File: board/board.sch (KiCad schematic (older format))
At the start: 22 parts, among them CON1 NRF24L01+MODULE, CON2 AVR-ISP-6, IC1 ATMEGA88PA-A, SW1 SW_PUSH, U1 XR1151

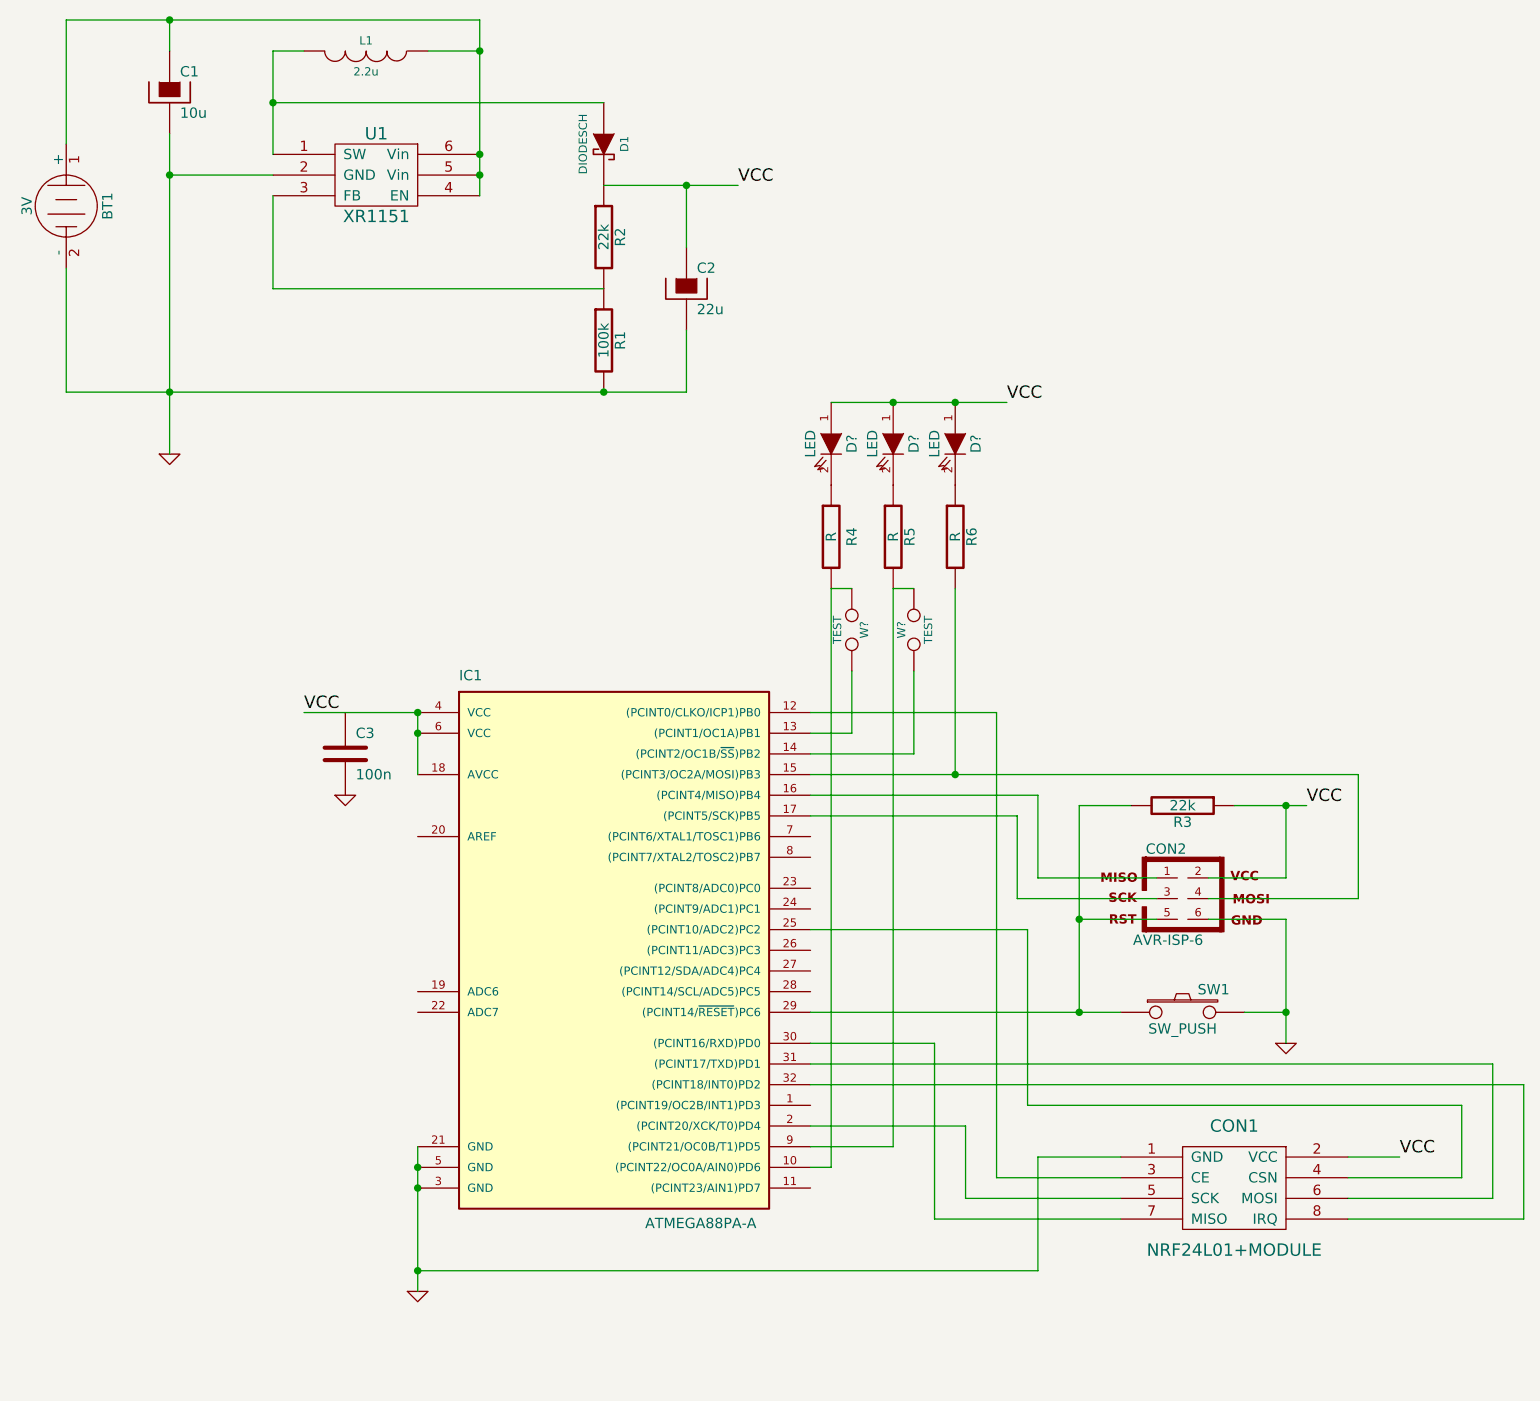
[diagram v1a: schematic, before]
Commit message: Replaced the 3 LEDs with a single 3-colour one
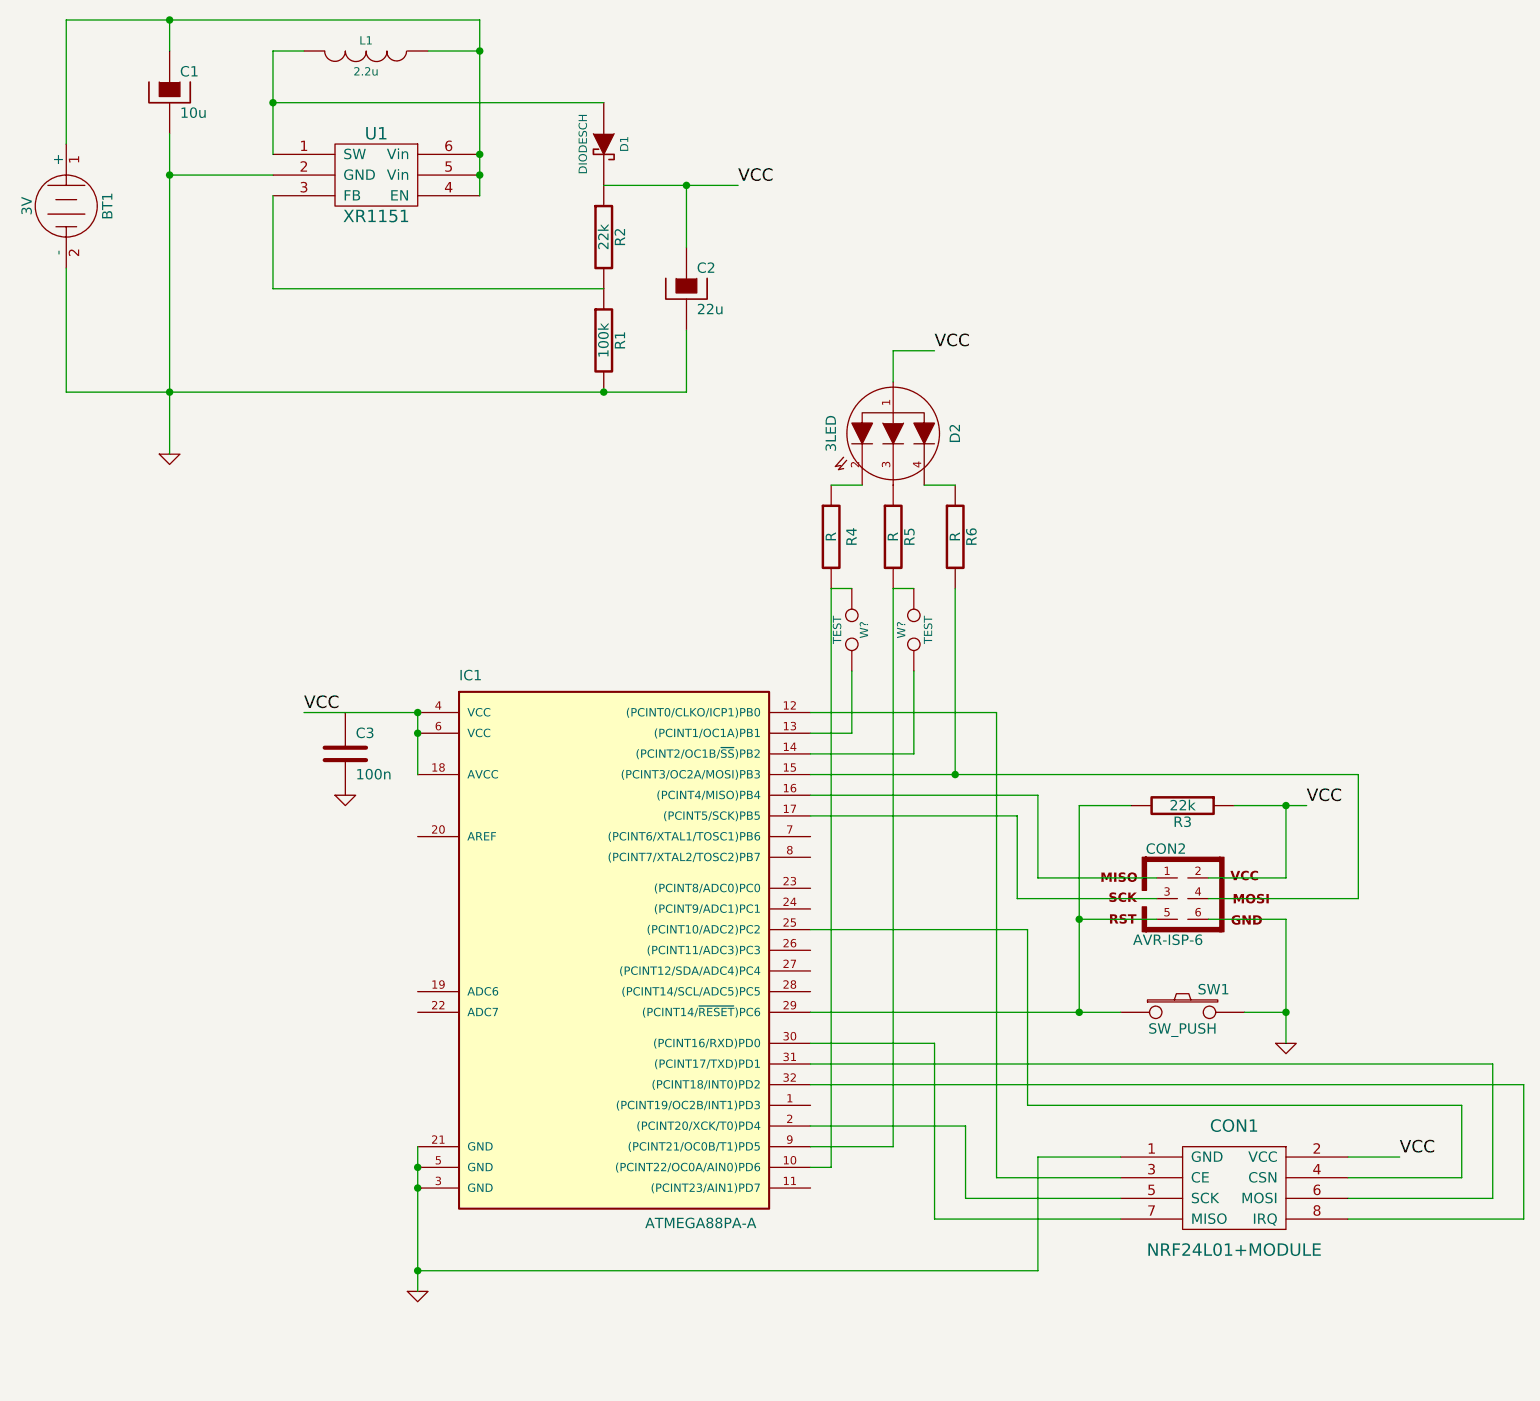
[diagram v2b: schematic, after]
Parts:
- removed D? (x3): LED, symbol LED
- added D2: 3LED, symbol 3LED
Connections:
- net VCC: now also D2.1 (A)
- net at R4.1: now also D2.2 (R)
- net at R5.1: now also D2.3 (G)
- net at R6.1: now also D2.4 (B)
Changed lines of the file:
@@
-EESchema Schematic File Version 2  date Tue 25 Mar 2014 21:10:04 CST
+EESchema Schematic File Version 2  date Tue 25 Mar 2014 21:40:07 CST
 LIBS:power
 LIBS:device
@@
 LIBS:nrf24l01+module
 LIBS:xr1151
+LIBS:3led
 LIBS:board-cache
 EELAYER 25  0
@@
 $EndDescr
 Wire Wire Line
-	4600 4650 5100 4650
-Wire Wire Line
-	5100 4650 5100 4250
-Wire Wire Line
-	5100 3850 5000 3850
-Wire Wire Line
-	4800 4250 4800 4550
-Wire Wire Line
-	4800 4550 4600 4550
-Wire Wire Line
-	4600 5500 5650 5500
-Wire Wire Line
-	5650 5500 5650 6350
-Wire Wire Line
-	5650 6350 7750 6350
-Wire Wire Line
-	7750 6350 7750 6700
+	5200 2700 5000 2700
+Wire Wire Line
+	5000 2700 5000 2850
+Wire Wire Line
+	4850 3350 4700 3350
+Wire Wire Line
+	4800 3850 4700 3850
+Wire Wire Line
+	7200 6700 7750 6700
+Wire Wire Line
+	1000 1100 3000 1100
+Wire Wire Line
+	1000 2900 4000 2900
+Wire Wire Line
+	1000 2900 1000 2300
+Connection ~ 5900 5900
+Wire Wire Line
+	4600 5900 6100 5900
+Wire Wire Line
+	6525 5350 7250 5350
+Wire Wire Line
+	7250 5350 7250 4750
+Wire Wire Line
+	6900 6050 6900 5450
+Wire Wire Line
+	6900 5450 6525 5450
+Wire Wire Line
+	5900 5900 5900 4900
+Wire Wire Line
+	6900 4900 6900 5250
+Wire Wire Line
+	6275 5250 5700 5250
+Connection ~ 5300 4750
+Wire Wire Line
+	7250 4750 4600 4750
+Wire Wire Line
+	7200 6900 8050 6900
+Wire Wire Line
+	8050 6900 8050 6250
+Wire Wire Line
+	8050 6250 4600 6250
+Wire Wire Line
+	5000 6550 5000 3850
+Wire Wire Line
+	5000 6550 4600 6550
+Wire Wire Line
+	6100 6600 5700 6600
+Wire Wire Line
+	5700 6600 5700 7150
+Connection ~ 2700 7150
+Wire Wire Line
+	5700 7150 2700 7150
+Wire Wire Line
+	4600 4450 5500 4450
+Wire Wire Line
+	5500 4450 5500 6700
+Wire Wire Line
+	5500 6700 6100 6700
+Wire Wire Line
+	4600 6050 5200 6050
+Wire Wire Line
+	5200 6050 5200 6900
+Wire Wire Line
+	5200 6900 6100 6900
+Connection ~ 2700 4450
+Connection ~ 2700 6650
+Wire Wire Line
+	2700 6550 2700 7250
+Connection ~ 3600 2900
+Wire Wire Line
+	4000 2900 4000 2600
+Connection ~ 1500 2900
+Wire Wire Line
+	1500 1250 1500 1100
+Wire Wire Line
+	2000 1750 2000 1250
+Wire Wire Line
+	2000 1250 2150 1250
+Wire Wire Line
+	2000 1950 2000 2400
+Wire Wire Line
+	2000 2400 3600 2400
+Connection ~ 3000 1750
+Connection ~ 3000 1850
+Wire Wire Line
+	2000 1850 1500 1850
+Connection ~ 3000 1250
+Wire Wire Line
+	3000 1250 2750 1250
+Wire Wire Line
+	3600 1500 2000 1500
+Connection ~ 2000 1500
+Wire Wire Line
+	1500 1650 1500 3200
+Connection ~ 1500 1850
+Wire Wire Line
+	4000 2200 4000 1900
+Wire Wire Line
+	2150 4450 2700 4450
+Wire Wire Line
+	4250 1900 3600 1900
+Connection ~ 4000 1900
+Connection ~ 2700 6750
+Wire Wire Line
+	6100 6800 5350 6800
+Wire Wire Line
+	5350 6800 5350 6450
+Wire Wire Line
+	5350 6450 4600 6450
+Wire Wire Line
+	4600 6650 4700 6650
+Wire Wire Line
+	4700 6650 4700 3850
+Wire Wire Line
+	5300 3850 5300 4750
+Wire Wire Line
+	7200 6600 7450 6600
+Wire Wire Line
+	4600 6150 7900 6150
+Wire Wire Line
+	7900 6150 7900 6800
+Wire Wire Line
+	7900 6800 7200 6800
+Wire Wire Line
+	5700 5250 5700 4850
+Wire Wire Line
+	5700 4850 4600 4850
+Wire Wire Line
+	6900 5250 6525 5250
+Wire Wire Line
+	4600 4950 5600 4950
+Wire Wire Line
+	5600 4950 5600 5350
+Wire Wire Line
+	5600 5350 6275 5350
+Wire Wire Line
+	5900 4900 6150 4900
+Wire Wire Line
+	6275 5450 5900 5450
+Connection ~ 5900 5450
+Wire Wire Line
+	6650 4900 7000 4900
+Connection ~ 6900 4900
+Wire Wire Line
+	6700 5900 6900 5900
+Connection ~ 6900 5900
+Wire Wire Line
+	1000 1100 1000 1700
+Connection ~ 1500 1100
+Wire Wire Line
+	3000 1100 3000 1950
+Wire Wire Line
+	2700 4450 2700 4750
 Connection ~ 2700 4550
 Wire Wire Line
-	2700 4750 2700 4450
-Wire Wire Line
-	3000 1950 3000 1100
-Connection ~ 1500 1100
-Wire Wire Line
-	1000 1700 1000 1100
-Connection ~ 6900 5900
-Wire Wire Line
-	6700 5900 6900 5900
-Connection ~ 6900 4900
-Wire Wire Line
-	6650 4900 7000 4900
-Connection ~ 5900 5450
-Wire Wire Line
-	6275 5450 5900 5450
-Wire Wire Line
-	6150 4900 5900 4900
-Wire Wire Line
-	6275 5350 5600 5350
-Wire Wire Line
-	5600 5350 5600 4950
-Wire Wire Line
-	5600 4950 4600 4950
-Wire Wire Line
-	6525 5250 6900 5250
-Wire Wire Line
-	4600 4850 5700 4850
-Wire Wire Line
-	5700 4850 5700 5250
-Wire Wire Line
-	7200 6800 7900 6800
-Wire Wire Line
-	7900 6800 7900 6150
-Wire Wire Line
-	7900 6150 4600 6150
-Wire Wire Line
-	7200 6600 7450 6600
-Connection ~ 5000 2950
-Wire Wire Line
-	5300 3850 5300 4750
-Wire Wire Line
-	4700 6650 4700 3850
-Wire Wire Line
-	4700 6650 4600 6650
-Wire Wire Line
-	4600 6450 5350 6450
-Wire Wire Line
-	5350 6450 5350 6800
-Wire Wire Line
-	5350 6800 6100 6800
-Connection ~ 2700 6750
-Connection ~ 4000 1900
-Wire Wire Line
-	4250 1900 3600 1900
-Wire Wire Line
-	2700 4450 2150 4450
-Wire Wire Line
-	4000 2200 4000 1900
-Connection ~ 1500 1850
-Wire Wire Line
-	1500 1650 1500 3200
-Connection ~ 2000 1500
-Wire Wire Line
-	3600 1500 2000 1500
-Wire Wire Line
-	3000 1250 2750 1250
-Connection ~ 3000 1250
-Wire Wire Line
-	2000 1850 1500 1850
-Connection ~ 3000 1850
-Connection ~ 3000 1750
-Wire Wire Line
-	3600 2400 2000 2400
-Wire Wire Line
-	2000 2400 2000 1950
-Wire Wire Line
-	2150 1250 2000 1250
-Wire Wire Line
-	2000 1250 2000 1750
-Wire Wire Line
-	1500 1250 1500 1100
-Connection ~ 1500 2900
-Wire Wire Line
-	4000 2600 4000 2900
-Connection ~ 3600 2900
-Wire Wire Line
-	2700 6550 2700 7250
-Connection ~ 2700 6650
-Connection ~ 2700 4450
-Wire Wire Line
-	6100 6900 5200 6900
-Wire Wire Line
-	5200 6900 5200 6050
-Wire Wire Line
-	5200 6050 4600 6050
-Wire Wire Line
-	6100 6700 5500 6700
-Wire Wire Line
-	5500 6700 5500 4450
-Wire Wire Line
-	5500 4450 4600 4450
-Wire Wire Line
-	2700 7150 5700 7150
-Connection ~ 2700 7150
-Wire Wire Line
-	5700 7150 5700 6600
-Wire Wire Line
-	5700 6600 6100 6600
-Wire Wire Line
-	4600 6550 5000 6550
-Wire Wire Line
-	5000 6550 5000 3850
-Wire Wire Line
-	5550 2950 4700 2950
-Connection ~ 5300 2950
-Wire Wire Line
-	4600 6250 8050 6250
-Wire Wire Line
-	8050 6250 8050 6900
-Wire Wire Line
-	8050 6900 7200 6900
-Wire Wire Line
-	4600 4750 7250 4750
-Connection ~ 5300 4750
-Wire Wire Line
-	5700 5250 6275 5250
-Wire Wire Line
-	6900 5250 6900 4900
-Wire Wire Line
-	5900 4900 5900 5900
-Wire Wire Line
-	6525 5450 6900 5450
-Wire Wire Line
-	6900 5450 6900 6050
-Wire Wire Line
-	7250 4750 7250 5350
-Wire Wire Line
-	7250 5350 6525 5350
-Wire Wire Line
-	4600 5900 6100 5900
-Connection ~ 5900 5900
-Wire Wire Line
-	1000 2300 1000 2900
-Wire Wire Line
-	1000 2900 4000 2900
-Wire Wire Line
-	1000 1100 3000 1100
-Wire Wire Line
-	7750 6700 7200 6700
-Wire Wire Line
-	4700 3850 4800 3850
+	7750 6700 7750 6350
+Wire Wire Line
+	7750 6350 5650 6350
+Wire Wire Line
+	5650 6350 5650 5500
+Wire Wire Line
+	5650 5500 4600 5500
+Wire Wire Line
+	4600 4550 4800 4550
+Wire Wire Line
+	4800 4550 4800 4250
+Wire Wire Line
+	5000 3850 5100 3850
+Wire Wire Line
+	5100 4250 5100 4650
+Wire Wire Line
+	5100 4650 4600 4650
+Wire Wire Line
+	5150 3350 5300 3350
+$Comp
+L 3LED D2
+U 1 1 533163B8
+P 5000 3100
+F 0 "D2" H 5000 3400 50  0000 C CNN
+F 1 "3LED" H 5000 2800 50  0000 C CNN
+	1    5000 3100
+	0    1    1    0
+$EndComp
 $Comp
 L TEST W?
@@
 Text Label 7450 6600 0    60   ~ 0
 VCC
-Text Label 5550 2950 0    60   ~ 0
+Text Label 5200 2700 0    60   ~ 0
 VCC
 $Comp
-L LED D?
-U 1 1 532D2F0F
-P 5300 3150
-F 0 "D?" H 5300 3250 50  0000 C CNN
-F 1 "LED" H 5300 3050 50  0000 C CNN
-	1    5300 3150
-	0    1    1    0
-$EndComp
-$Comp
-L LED D?
-U 1 1 532D2F02
-P 5000 3150
-F 0 "D?" H 5000 3250 50  0000 C CNN
-F 1 "LED" H 5000 3050 50  0000 C CNN
-	1    5000 3150
-	0    1    1    0
-$EndComp
-$Comp
-L LED D?
-U 1 1 532D2EEF
-P 4700 3150
-F 0 "D?" H 4700 3250 50  0000 C CNN
-F 1 "LED" H 4700 3050 50  0000 C CNN
-	1    4700 3150
-	0    1    1    0
-$EndComp
-$Comp
 L R R6

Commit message: Replace the ATmega8 test points with solder pads
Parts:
- removed W? (x2): TEST, symbol TEST
- added L1, L2: JOIN, symbol JOIN
- added L3, L4: BREAK, symbol BREAK
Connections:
- net at IC1.10 ((PCINT22/OC0A/AIN0)PD6): now also L1.1; no longer R4.2
- net at IC1.13 ((PCINT1/OC1A)PB1): now also L3.1
- net at IC1.14 ((PCINT2/OC1B/~SS~)PB2): now also L4.1
- net at IC1.9 ((PCINT21/OC0B/T1)PD5): now also L2.1; no longer R5.2
- new net: L1.2, L3.2, R4.2
- new net: L2.2, L4.2, R5.2
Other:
- moved on the sheet: D2, R4, R5, R6
